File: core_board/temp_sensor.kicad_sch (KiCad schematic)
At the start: 0 parts

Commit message: Add temp sensor
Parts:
- added C11: 100nF, MRDT_Shields:RoveNode_H5, symbol Device:C
- added R16: 10kohm, Package_SO:TSSOP-20_4.4x6.5mm_P0.65mm, symbol Device:R_US
- added TH1: Thermistor_NTC, Package_DFN_QFN:Nordic_AQFN-94-1EP_7x7mm_P0.4mm, symbol Device:Thermistor_NTC
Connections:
- new net +3V3: R16.1
- new net GND: C11.2, TH1.2
- new net TEMP_OUT: C11.1, R16.2, TH1.1

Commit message: Finish Schematic
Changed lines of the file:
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@@
 	(paper "A4")
-	(junction
-		(at 139.7 81.28)
-		(diameter 0)
-		(color 0 0 0 0)
-	)
-	(junction
-		(at 129.54 97.79)
-		(diameter 0)
-		(color 0 0 0 0)
-	)
 	(junction
 		(at 134.62 111.76)
@@
 	)
 	(junction
-		(at 139.7 96.52)
-		(diameter 0)
-		(color 0 0 0 0)
-	)
-	(junction
 		(at 139.7 93.98)
-		(diameter 0)
-		(color 0 0 0 0)
-	)
-	(junction
-		(at 139.7 104.14)
-		(diameter 0)
-		(color 0 0 0 0)
-	)
-	(junction
-		(at 139.7 88.9)
-		(diameter 0)
-		(color 0 0 0 0)
-	)
-	(junction
-		(at 139.7 71.12)
-		(diameter 0)
-		(color 0 0 0 0)
-	)
-	(junction
-		(at 129.54 105.41)
 		(diameter 0)
 		(color 0 0 0 0)
@@
 	(wire
 		(pts
-			(xy 129.54 93.98) (xy 129.54 101.6)
-		)
-		(stroke
-			(width 0)
-			(type default)
-		)
-	)
-	(wire
-		(pts
 			(xy 139.7 71.12) (xy 139.7 81.28)
-		)
-		(stroke
-			(width 0)
-			(type default)
-		)
-	)
-	(wire
-		(pts
-			(xy 139.7 96.52) (xy 139.7 97.79)
 		)
 		(stroke
@@
 	(wire
 		(pts
-			(xy 139.7 81.28) (xy 139.7 82.55)
-		)
-		(stroke
-			(width 0)
-			(type default)
-		)
-	)
-	(wire
-		(pts
-			(xy 129.54 104.14) (xy 129.54 105.41)
-		)
-		(stroke
-			(width 0)
-			(type default)
-		)
-	)
-	(wire
-		(pts
 			(xy 139.7 104.14) (xy 139.7 111.76)
-		)
-		(stroke
-			(width 0)
-			(type default)
-		)
-	)
-	(wire
-		(pts
-			(xy 139.7 87.63) (xy 139.7 88.9)
-		)
-		(stroke
-			(width 0)
-			(type default)
-		)
-	)
-	(wire
-		(pts
-			(xy 139.7 102.87) (xy 139.7 104.14)
 		)
 		(stroke
@@
 	(wire
 		(pts
-			(xy 139.7 68.58) (xy 139.7 71.12)
+			(xy 129.54 93.98) (xy 129.54 97.79)
 		)
 		(stroke

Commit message: add
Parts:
- renumbered C11 to C10, R16 to R7
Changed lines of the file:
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@@
 		(dnp no)
 		(fields_autoplaced yes)
-		(property "Reference" "#PWR062"
+		(property "Reference" "#PWR022"
 			(at 139.7 74.93 0)
 			(hide yes)
@@
 			(project "core_board"
 				(path "/e01d6047-065c-44c8-9643-8ab57e6ffae6/77f19b6f-fa72-4932-9cd3-32a2305647f7"
-					(reference "#PWR062")
+					(reference "#PWR022")
 					(unit 1)
 				)
@@
 		(dnp no)
 		(fields_autoplaced yes)
-		(property "Reference" "#PWR061"
+		(property "Reference" "#PWR021"
 			(at 134.62 123.19 0)
 			(hide yes)
@@
 			(project "core_board"
 				(path "/e01d6047-065c-44c8-9643-8ab57e6ffae6/77f19b6f-fa72-4932-9cd3-32a2305647f7"
-					(reference "#PWR061")
+					(reference "#PWR021")
 					(unit 1)
 				)
@@
 		(in_pos_files yes)
 		(dnp no)
-		(property "Reference" "C11"
+		(property "Reference" "C10"
 			(at 124.46 99.06 0)
 			(show_name no)
@@
 			(project "core_board"
 				(path "/e01d6047-065c-44c8-9643-8ab57e6ffae6/77f19b6f-fa72-4932-9cd3-32a2305647f7"
-					(reference "C11")
+					(reference "C10")
 					(unit 1)
 				)
@@
 		(dnp no)
 		(fields_autoplaced yes)
-		(property "Reference" "R16"
+		(property "Reference" "R7"
 			(at 142.24 83.8199 0)
 			(show_name no)
@@
 			(project "core_board"
 				(path "/e01d6047-065c-44c8-9643-8ab57e6ffae6/77f19b6f-fa72-4932-9cd3-32a2305647f7"
-					(reference "R16")
-					(unit 1)
-				)
+					(reference "R7")
+					(unit 1)
+				)

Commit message: Almost done with Schematic
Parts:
- C10: footprint MRDT_Shields:RoveNode_H5 -> Capacitor_SMD:C_0603_1608Metric_Pad1.08x0.95mm_HandSolder
- R7: footprint Package_SO:TSSOP-20_4.4x6.5mm_P0.65mm -> Resistor_SMD:R_0603_1608Metric_Pad0.98x0.95mm_HandSolder
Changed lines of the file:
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@@
 			)
 		)
-		(property "Footprint" "MRDT_Shields:RoveNode_H5"
+		(property "Footprint" "Capacitor_SMD:C_0603_1608Metric_Pad1.08x0.95mm_HandSolder"
 			(at 130.5052 105.41 0)
 			(hide yes)
@@
 			)
 		)
-		(property "Footprint" "Package_SO:TSSOP-20_4.4x6.5mm_P0.65mm"
+		(property "Footprint" "Resistor_SMD:R_0603_1608Metric_Pad0.98x0.95mm_HandSolder"
 			(at 140.716 85.344 90)
 			(hide yes)

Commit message: Add extra components
fixed LED connector
removed extra buck
fixed wrong footprints
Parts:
- TH1: footprint Package_DFN_QFN:Nordic_AQFN-94-1EP_7x7mm_P0.4mm -> Resistor_SMD:R_1206_3216Metric_Pad1.30x1.75mm_HandSolder
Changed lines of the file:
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@@
 			)
 		)
-		(property "Footprint" "Package_DFN_QFN:Nordic_AQFN-94-1EP_7x7mm_P0.4mm"
+		(property "Footprint" "Resistor_SMD:R_1206_3216Metric_Pad1.30x1.75mm_HandSolder"
 			(at 139.7 99.06 0)
 			(hide yes)

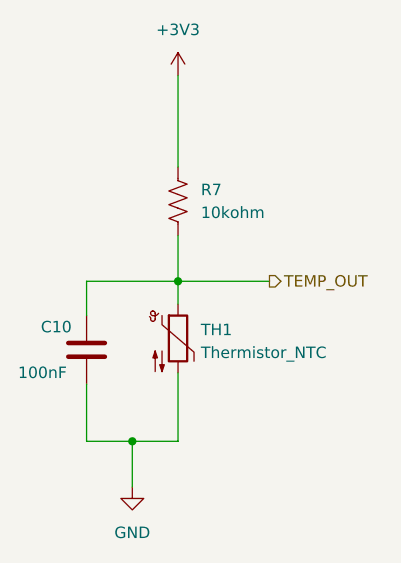
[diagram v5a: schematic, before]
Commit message: add datasheet
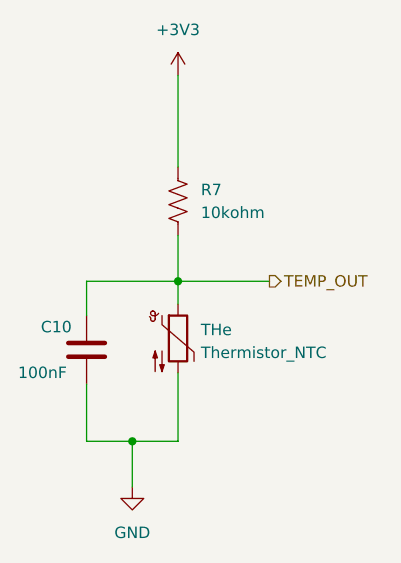
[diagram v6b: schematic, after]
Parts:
- renumbered TH1 to THe
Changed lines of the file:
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@@
 		(dnp no)
 		(fields_autoplaced yes)
-		(property "Reference" "TH1"
+		(property "Reference" "THe"
 			(at 142.24 99.3774 0)
 			(show_name no)
@@
 			)
 		)
-		(property "Datasheet" ""
+		(property "Datasheet" "https://www.tdk-electronics.tdk.com/inf/50/db/ntc/NTC_SMD_Standard_series_0402.pdf"
 			(at 139.7 99.06 0)
 			(hide yes)
@@
 			(project "core_board"
 				(path "/e01d6047-065c-44c8-9643-8ab57e6ffae6/77f19b6f-fa72-4932-9cd3-32a2305647f7"
-					(reference "TH1")
+					(reference "THe")
 					(unit 1)
 				)

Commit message: Fix buck circuit values
nothing had values, so I added them
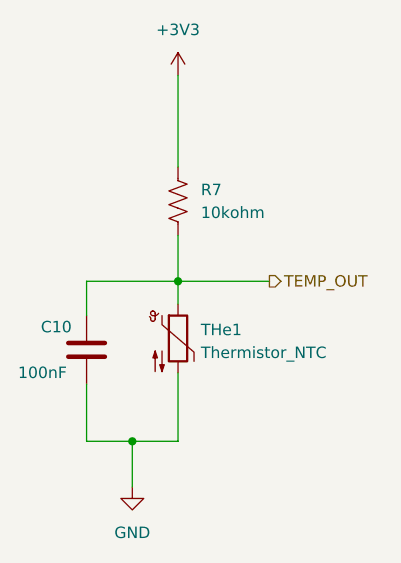
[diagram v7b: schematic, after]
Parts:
- renumbered THe to THe1
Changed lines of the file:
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@@
 		(dnp no)
 		(fields_autoplaced yes)
-		(property "Reference" "THe"
+		(property "Reference" "THe1"
 			(at 142.24 99.3774 0)
 			(show_name no)
@@
 			(project "core_board"
 				(path "/e01d6047-065c-44c8-9643-8ab57e6ffae6/77f19b6f-fa72-4932-9cd3-32a2305647f7"
-					(reference "THe")
+					(reference "THe1")
 					(unit 1)
 				)
